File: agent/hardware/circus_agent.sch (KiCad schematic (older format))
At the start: 59 parts

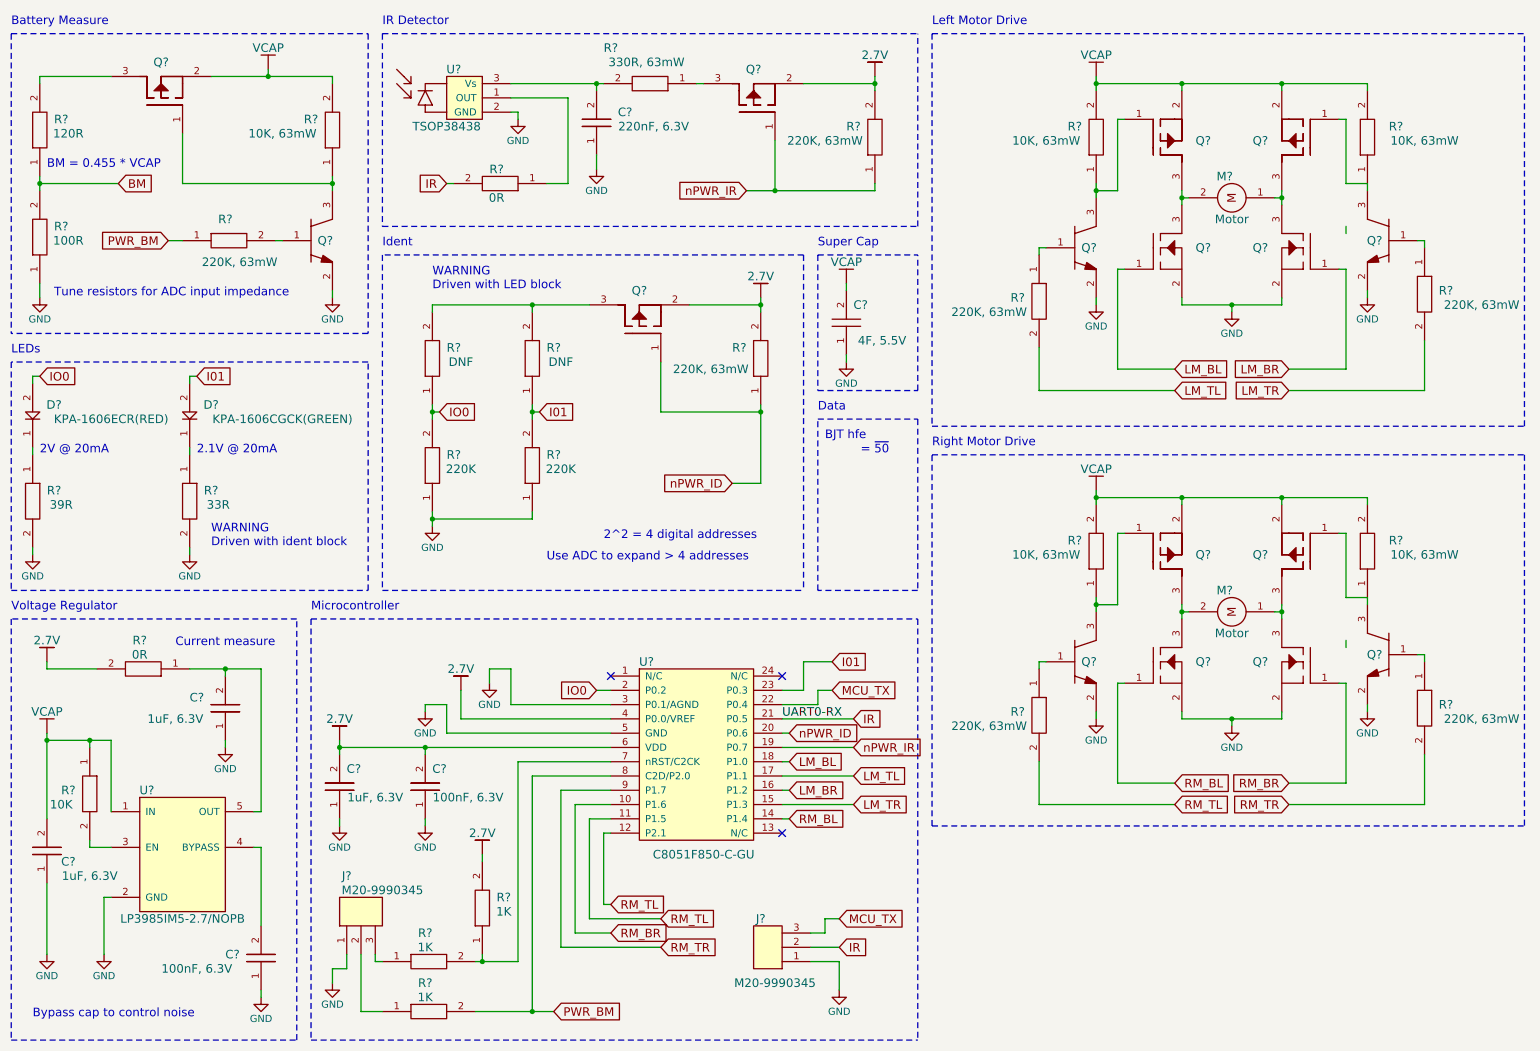
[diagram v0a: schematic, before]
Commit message: designators and pass erc
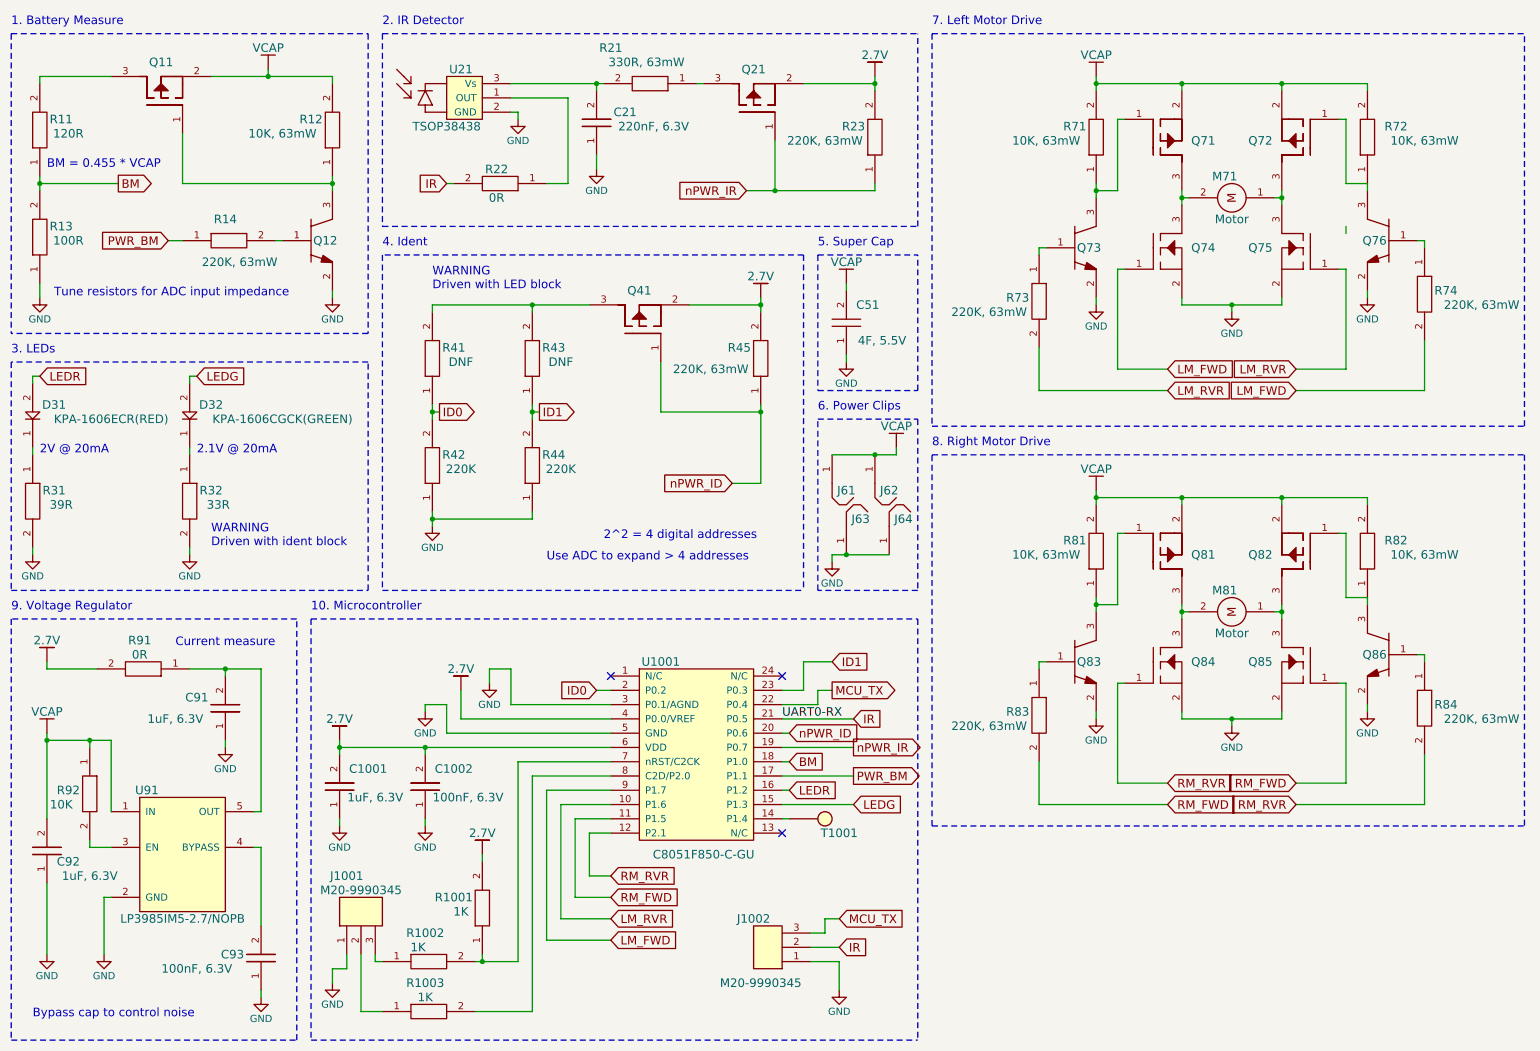
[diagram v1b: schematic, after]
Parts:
- removed C?: 4F, 5.5V, symbol SuperCap
- removed J? (x2): M20-9990345, symbol M20-9990345
- removed U?: TSOP38438, symbol TSOP38438
- added C51: 4F, 5.5V, symbol SuperCap
- added J1001, J1002: M20-9990345, symbol M20-9990345
- added J61, J62, J63, J64: PowerClip, symbol PowerClip
- added T1001: TestPoint, symbol TestPoint
- added U21: TSOP38438, symbol TSOP38438
- gave numbers to parts that had none: 55
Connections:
- net BM: now also U1001.18 (P1.0)
- net GND: now also C51.1, J1001.1, J1002.1, J63.1, J64.1, U21.2 (GND)
- net IR: now also J1002.2
- net MCU_TX: now also J1002.3
- net PWR_BM: now also U1001.17 (P1.1); no longer R1003.2, U1001.8 (C2D/P2.0)
- net at R22.1: now also U21.1 (OUT)
- net at C21.2, R21.2: now also U21.3 (Vs)
- net at R1002.1: now also J1001.3
- net at R1003.1: now also J1001.2
- net I01 renamed ID1
- net ID1: no longer D32.2
- net IO0 renamed ID0
- net ID0: no longer D31.2
- net LM_BL renamed LM_FWD
- net LM_FWD: now also R74.2, U1001.9 (P1.7); no longer U1001.18 (P1.0)
- net LM_BR renamed LEDR
- net LEDR: now also D31.2; no longer Q75.1
- net LM_TL renamed LM_RVR
- net LM_RVR: now also Q75.1, U1001.10 (P1.6); no longer U1001.17 (P1.1)
- net LM_TR renamed LEDG
- net LEDG: now also D32.2; no longer R74.2
- net RM_BL: no longer names the net of U1001.14 (P1.4)
- net RM_BL: now also T1001.~; no longer Q84.1
- net RM_BR renamed RM_FWD
- net RM_FWD: now also R83.2, U1001.11 (P1.5); no longer U1001.10 (P1.6)
- removed net RM_TL: R83.2, U1001.11 (P1.5), U1001.12 (P2.1)
- net RM_TR renamed RM_RVR
- net RM_RVR: now also Q84.1, U1001.12 (P2.1); no longer U1001.9 (P1.7)
- new net: R1003.2, U1001.8 (C2D/P2.0)
- new net: J61.1, J62.1
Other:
- note added: "1. Battery Measure"
- note added: "10. Microcontroller"
- note added: "2. IR Detector"
- note added: "3. LEDs\n"
- note added: "4. Ident"
- note added: "5. Super Cap"
- note added: "6. Power Clips"
- note added: "7. Left Motor Drive"
- note added: "8. Right Motor Drive"
- note added: "9. Voltage Regulator"
- note removed: "= ~50"
- note removed: "BJT hfe"
- note removed: "Battery Measure"
- note removed: "Data"
- note removed: "IR Detector"
- note removed: "Ident"
- note removed: "LEDs\n"
- note removed: "Left Motor Drive"
- note removed: "Microcontroller"
- note removed: "Right Motor Drive"
- note removed: "Super Cap"
- note removed: "Voltage Regulator"

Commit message: temp footprint and charge detection
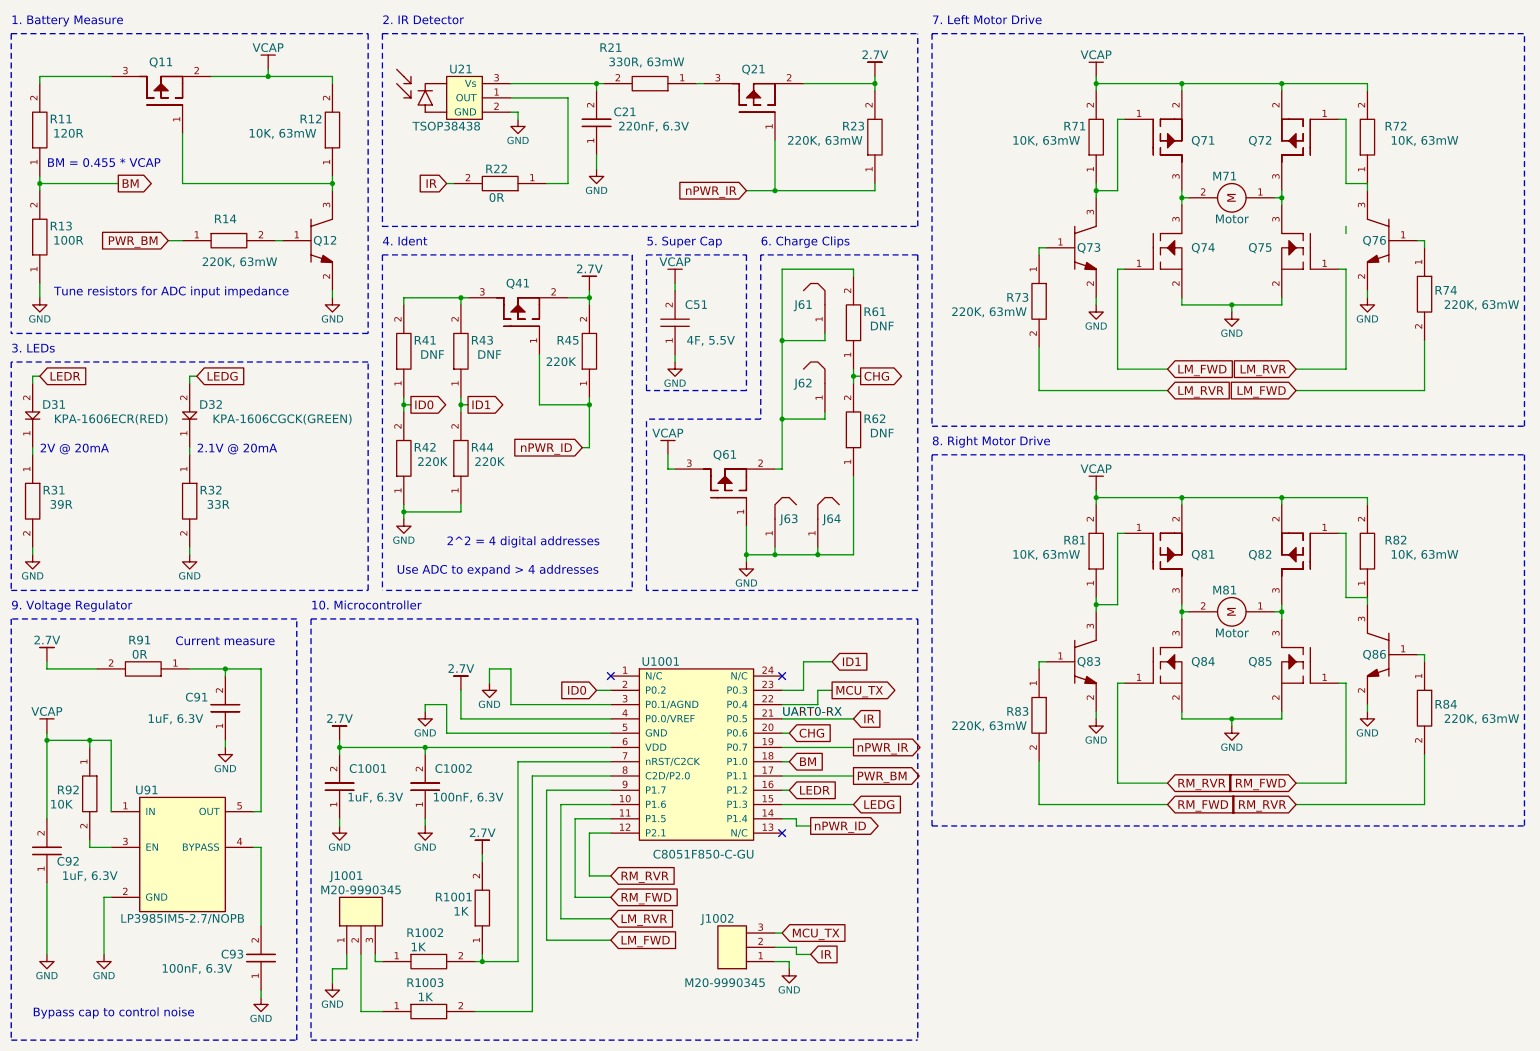
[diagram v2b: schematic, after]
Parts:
- removed T1001: TestPoint, symbol TestPoint
- added Q61: PMV65XPEA, symbol PMV65XPEA
- added R61, R62: DNF, symbol CRCW0402330RFKED
- R45: value 220K, 63mW -> 220K
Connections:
- net GND: now also Q61.1, R62.1
- net nPWR_ID: now also U1001.14 (P1.4); no longer U1001.20 (P0.6)
- net at J61.1, J62.1: now also Q61.2, R61.2
- new net CHG: R61.1, R62.2, U1001.20 (P0.6)
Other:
- note added: "6. Charge Clips"
- note removed: "6. Power Clips"
- note removed: "WARNING\nDriven with LED block"
- note removed: "WARNING\nDriven with ident block"
- moved on the sheet: C51, J1002, J61, J62, J63, J64, Q41, R41, R42, R43, R44, R45

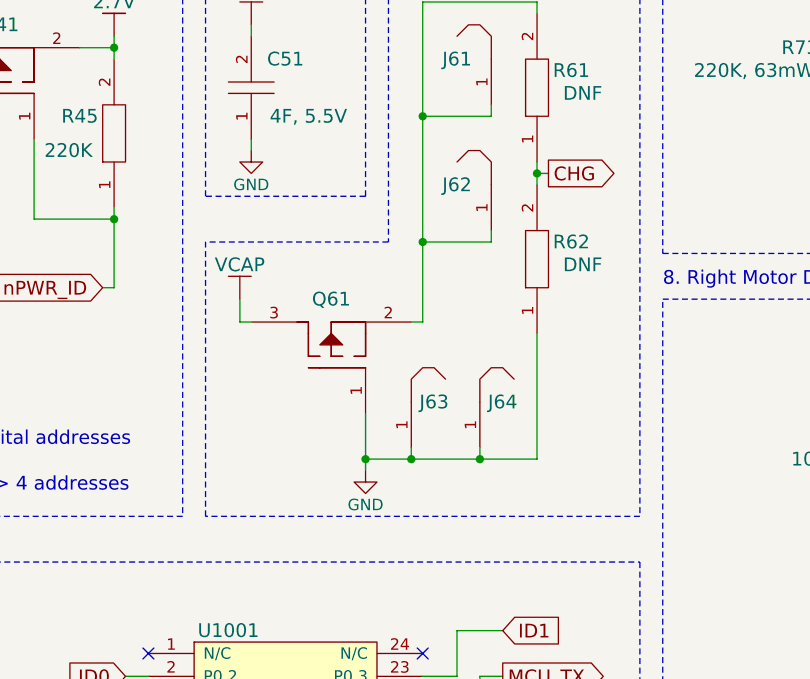
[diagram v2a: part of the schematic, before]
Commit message: Motor, cap footprints and remove reverse fet
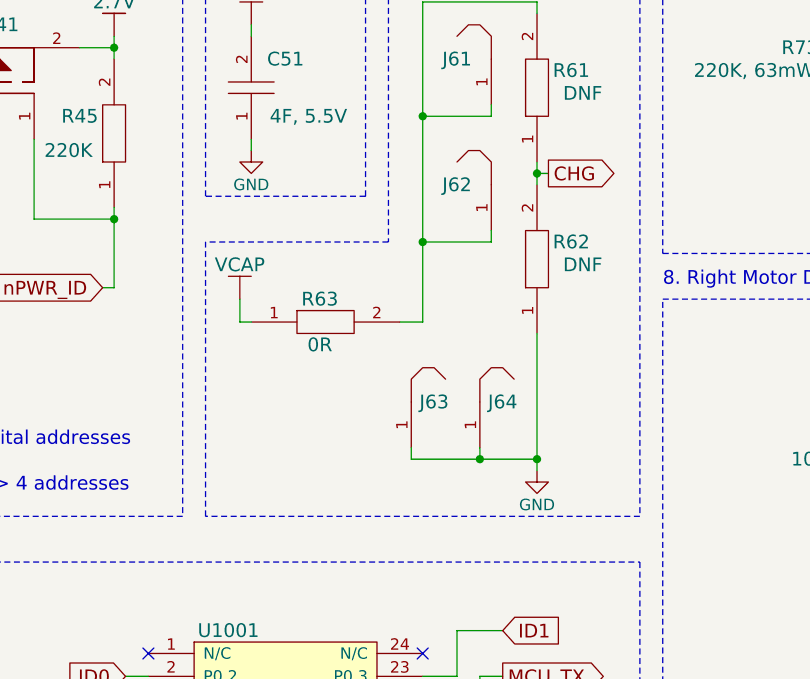
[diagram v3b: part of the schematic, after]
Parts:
- removed Q61: PMV65XPEA, symbol PMV65XPEA
- added R63: 0R, circus_agent:0402, symbol CRCW0402330RFKED
- C1001, C1002, C21, C91, C92, C93, R1001, R1002, R1003, R11, R12, R13, R14, R21, R22, R23, R31, R32, R41, R42, R43, R44, R45, R61, R62, R71, R72, R73, R74, R81, R82, R83, R84, R91, R92: footprint (none) -> circus_agent:0402
- D31, D32: footprint (none) -> circus_agent:KPA
- J1001, J1002: footprint (none) -> circus_agent:M20-9990345
- J61, J62, J63, J64: footprint (none) -> circus_agent:PowerClip
- Q11, Q21, Q41, Q71, Q72, Q81, Q82: footprint (none) -> circus_agent:PMV65XPEA
- Q12, Q73, Q76, Q83, Q86: footprint (none) -> circus_agent:MMBT2222LT1G
- Q74, Q75, Q84, Q85: footprint (none) -> circus_agent:IRLML6244TRPBF
- U1001: footprint (none) -> circus_agent:C8051F850-C-GU
- U21: footprint (none) -> circus_agent:TSOP38438
- U91: footprint (none) -> circus_agent:LP3985
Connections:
- net at J61.1, J62.1, R61.2: now also R63.2
